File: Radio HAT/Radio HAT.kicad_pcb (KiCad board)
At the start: 2 copper layers, 65 x 35 mm, 15 parts, among them J1 Raspberry_Pi_2_3, J2 Coax SMA, J3 Barrel_Jack, U1 RFM98PW, U2 AZ2185D-ADJTRG1

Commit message: Finished board design
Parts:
- moved C3 14.3 mm to (104.0, 125.0), turned to -90 degrees
- moved C4 14.3 mm to (104.0, 131.0), turned to 90 degrees
- moved R3 14.3 mm to (117.0, 131.0), turned to 90 degrees
- moved R4 14.3 mm to (117.0, 125.0), turned to 90 degrees
- moved R1 7.07 mm to (113.0, 112.0), turned to 90 degrees
- moved R2 4.47 mm to (116.0, 112.0), turned to 90 degrees
- moved U2 2.13 mm to (110.3, 129.0), turned to -90 degrees
- moved J2 0.60 mm to (155.6, 130.0)
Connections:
- net Net-(J2-In) renamed /RF_ANT
- net Net-(U2-ADJ) renamed /REG_ADJ
- J1 pad 1: PI_3V3 -> unconnected-(J1-3V3-Pad1)
- J1 pad 13: /RF_DIO5 -> unconnected-(J1-GPIO27-Pad13)
- J1 pad 15: /RF_DIO0 -> unconnected-(J1-GPIO22-Pad15)
- J1 pad 16: /RF_DIO1 -> unconnected-(J1-GPIO23-Pad16)
- J1 pad 17: PI_3V3 -> unconnected-(J1-3V3-Pad17)
- J1 pad 18: /RF_DIO2 -> unconnected-(J1-GPIO24-Pad18)
- J1 pad 2: PI_5V -> unconnected-(J1-5V-Pad2)
- J1 pad 22: /RF_DIO3 -> unconnected-(J1-GPIO25-Pad22)
- J1 pad 33: unconnected-(J1-PWM1/GPIO13-Pad33) -> /RF_DIO3
- J1 pad 35: unconnected-(J1-GPIO19/MISO1-Pad35) -> /RF_DIO0
- J1 pad 36: unconnected-(J1-GPIO16-Pad36) -> /RF_DIO5
- J1 pad 38: unconnected-(J1-GPIO20/MOSI1-Pad38) -> /RF_DIO1
- J1 pad 4: PI_5V -> unconnected-(J1-5V-Pad4)
- J1 pad 40: unconnected-(J1-GPIO21/SCLK1-Pad40) -> /RF_DIO2
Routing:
- net +6V: track 0.00 -> 69.6 mm, vias 0 -> 2
- net /RF_RESET: track 0.00 -> 46.2 mm
- net /RF_DIO5: track 0.00 -> 40.1 mm, vias 0 -> 1
- net /RF_CS: track 0.00 -> 32.6 mm
- net /RF_SCK: track 0.00 -> 24.2 mm
- net /RF_DIO3: track 0.00 -> 23.4 mm
- net /RF_MISO: track 0.00 -> 19.8 mm
- net /RF_MOSI: track 0.00 -> 19.3 mm, vias 0 -> 1
- net /RF_DIO4: track 0.00 -> 17.8 mm, vias 0 -> 1
- net /RF_DIO0: track 0.00 -> 16.3 mm
- net VCC: track 0.00 -> 15.7 mm
- net /REG_ADJ: track 0.00 -> 11.7 mm
- net +3V3: track 0.00 -> 10.5 mm
- net /RF_DIO1: track 0.00 -> 8.31 mm
- net /RF_ANT: track 0.00 -> 6.50 mm
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- added copper zone on B.Cu, net GND
- added copper zone on F.Cu, net GND
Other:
- board text added: "AZ2185"
- board text added: "Argus-1 Ground Station"
- board text added: "Carnegie Mellon ECE"
- board text added: "JLCJLCJLCJLC"
- board text added: "RFM98PW"

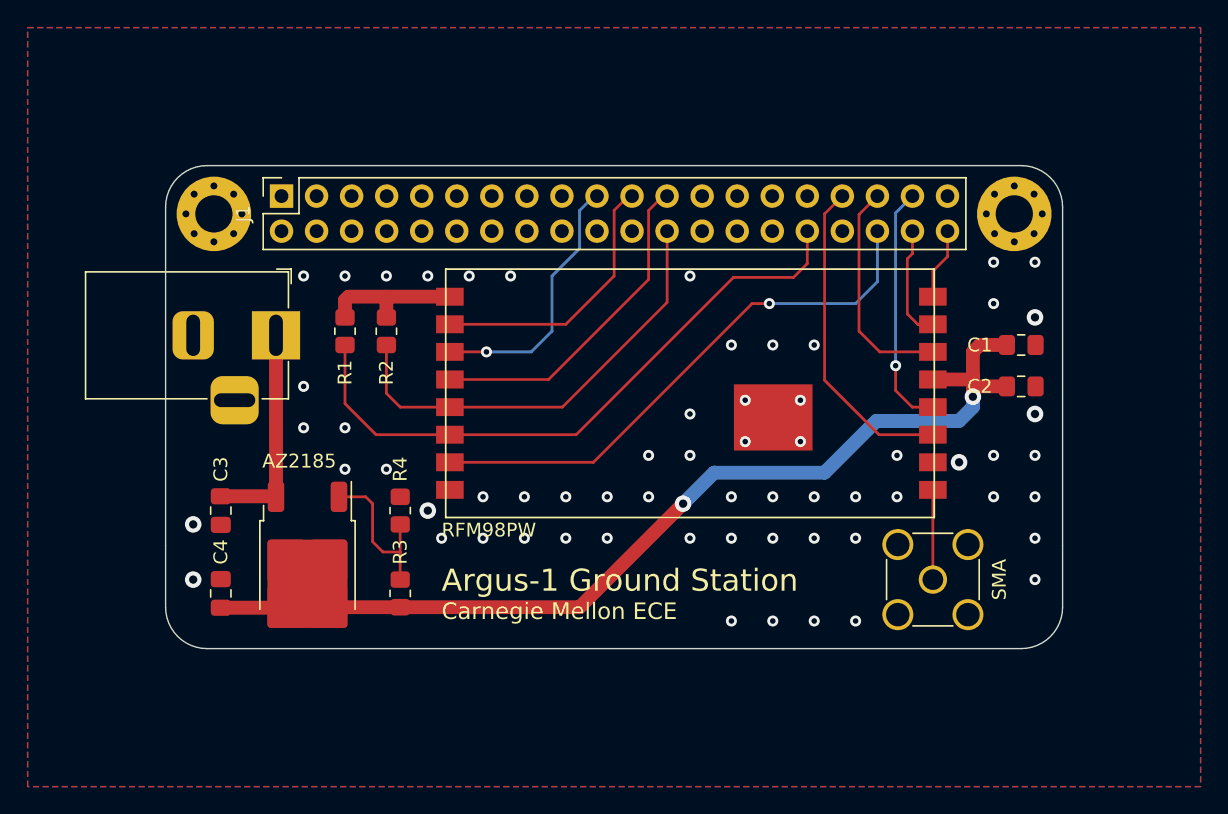
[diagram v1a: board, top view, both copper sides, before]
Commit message: Implemented changes from PR review
Changes implemented:
 - added schematic documentation and page settings
 - fixed PCB silkscreen
 - added board rev. and information on back silkscreen
 - added 3D models, generated 3D model for board
 - generated HTML BOM
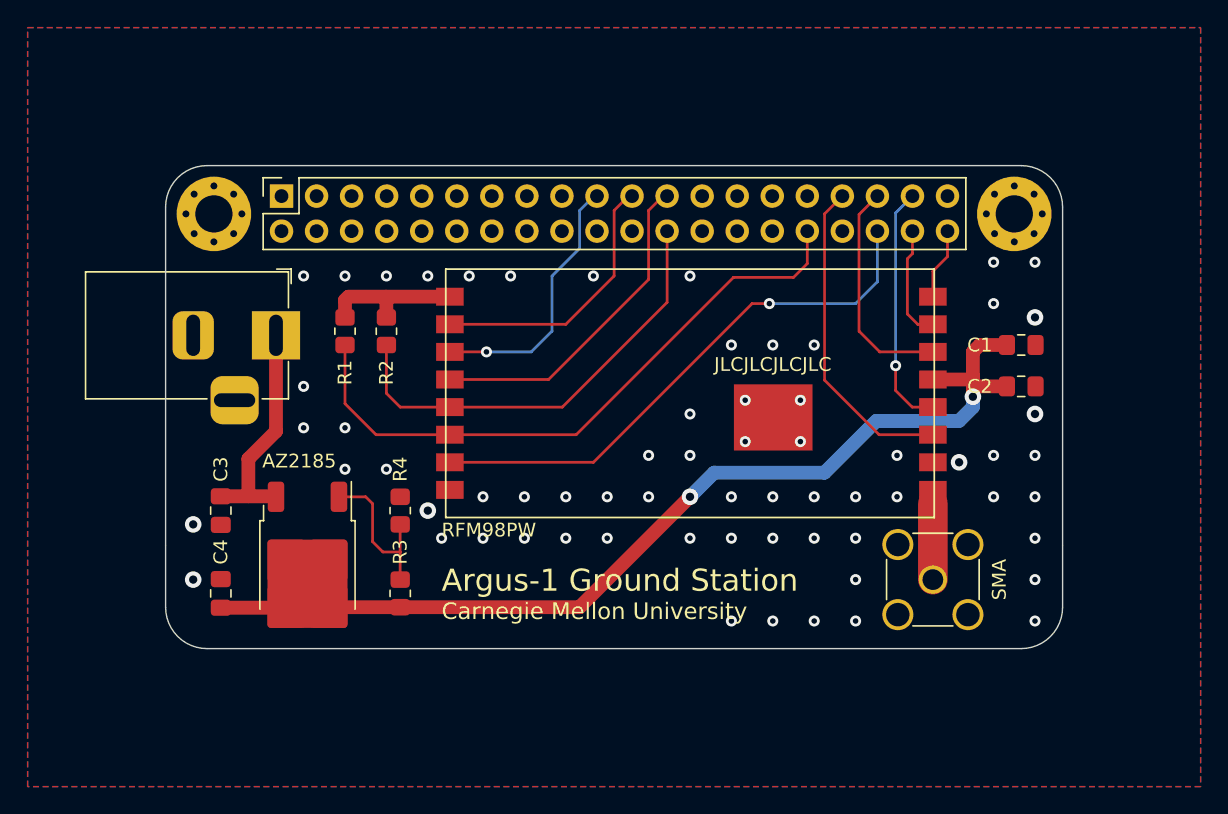
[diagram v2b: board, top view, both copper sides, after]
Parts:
- U1: footprint Mainboard:RFM95PW -> RF_Module_HOPERF:RFM95PW
- U2: value AZ2185D-ADJTRG1 -> AZ2185D-ADJTRG1
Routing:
- net VCC: track 15.7 -> 16.5 mm
- net GND: vias 62 -> 65
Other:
- board text added: "Argus-1 Groundstation v1.0"
- board text added: "CMU Spacecraft Design-Build-Fly 2023"
- board text added: "Carnegie Mellon University"
- board text added: "Comms-Ops Team Designer: Akshat Sahay"
- board text removed: "Carnegie Mellon ECE"

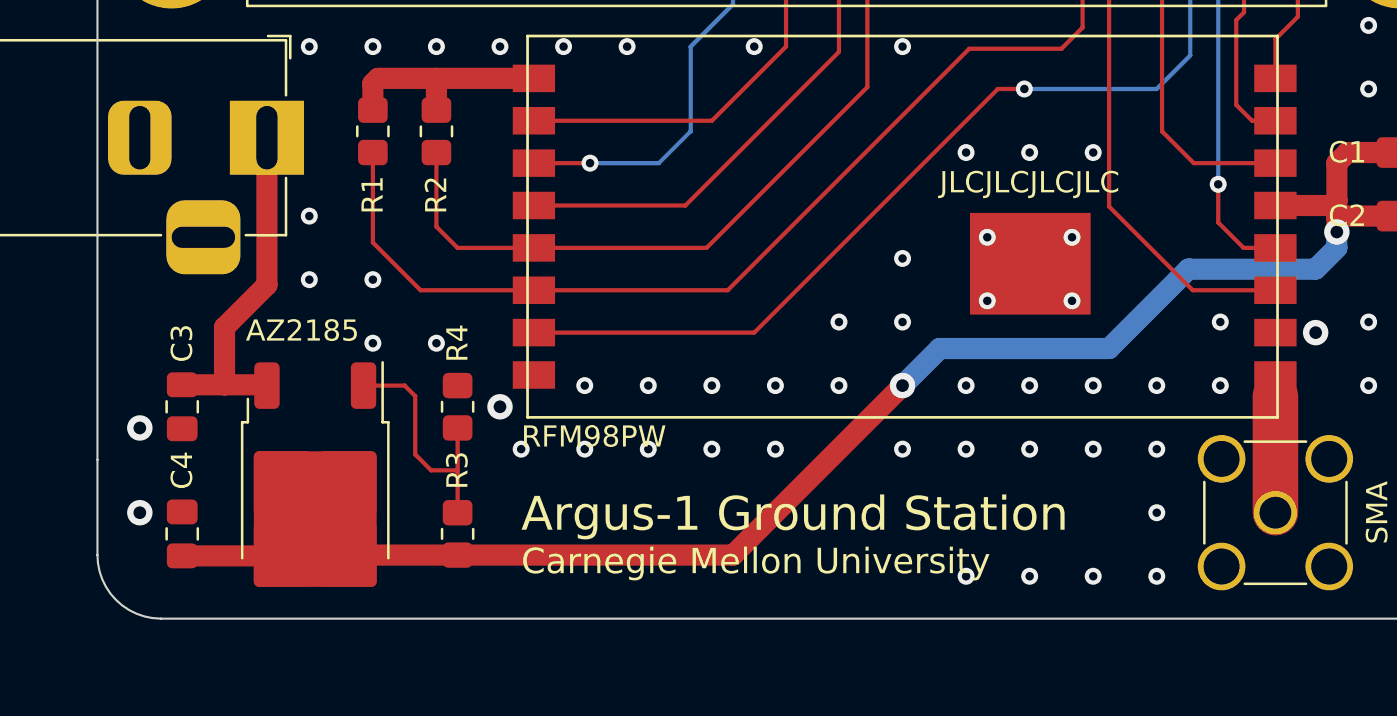
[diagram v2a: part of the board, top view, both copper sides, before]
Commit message: Implemented changes from PR
Fixed 3D models of board, added testpoints on board.
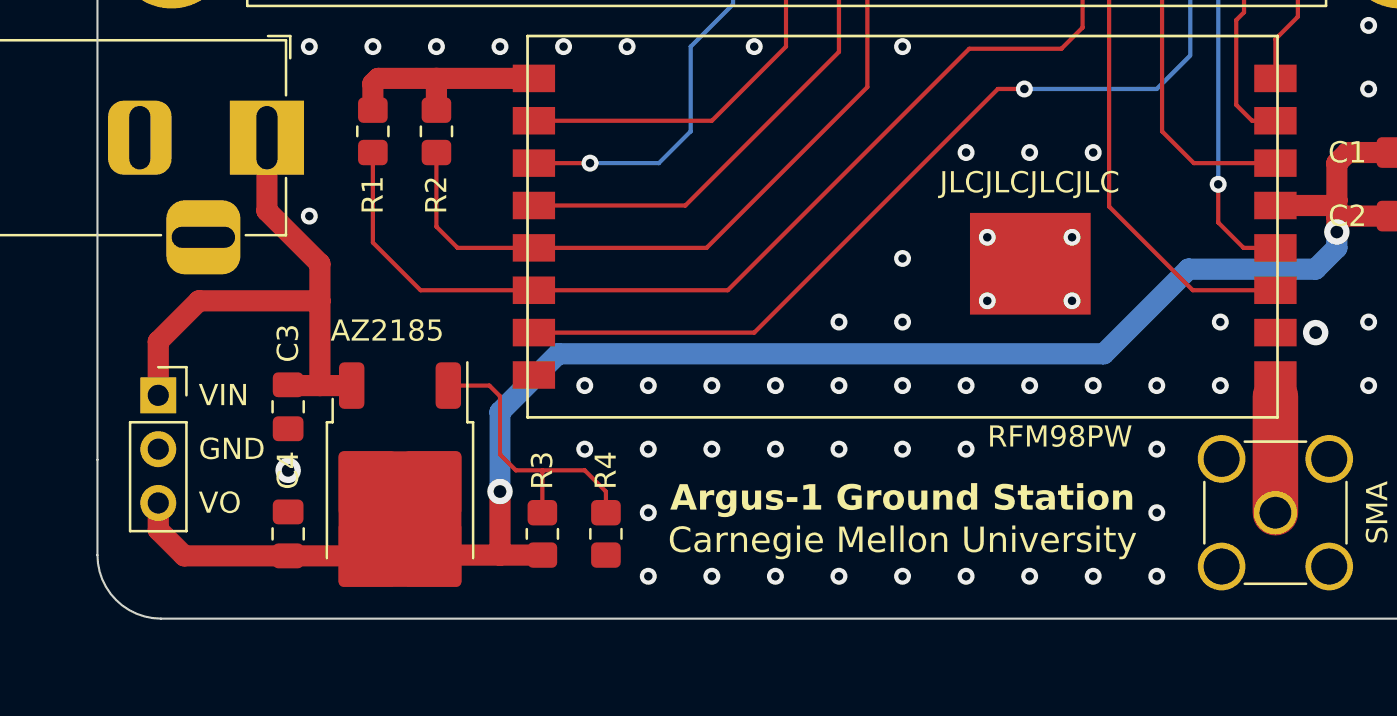
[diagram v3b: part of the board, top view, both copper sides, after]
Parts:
- added J4: Testpoints, Connector_PinSocket_2.54mm:PinSocket_1x03_P2.54mm_Vertical, F.Cu at (102.9, 124.5)
- moved R4 9.22 mm to (124.0, 131.0), turned to -90 degrees
- moved C3 5.00 mm to (109.0, 125.0)
- moved C4 5.00 mm to (109.0, 131.0)
- moved R3 4.00 mm to (121.0, 131.0)
- moved U2 4.00 mm to (114.3, 129.0)
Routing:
- net VCC: track 16.5 -> 26.8 mm
- net +6V: track 69.6 -> 78.5 mm
- net /REG_ADJ: track 11.7 -> 14.1 mm
- net GND: vias 65 -> 63
- net (no net): vias 0 -> 1
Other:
- board text added: "GND"
- board text added: "VIN"
- board text added: "VO"
